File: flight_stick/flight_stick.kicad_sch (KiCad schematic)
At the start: 61 parts, among them J1 Load Cell 1, J10 USB_C_Receptacle_USB2.0, J11 Conn_01x05_Pin, J3 Load Cell 2, J5 Load Cell 3, J7 Conn_01x04_Male, J8 Conn_01x05_Pin, J9 Conn_ST_STDC14, Q4 2N7002, Q5 2N7002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

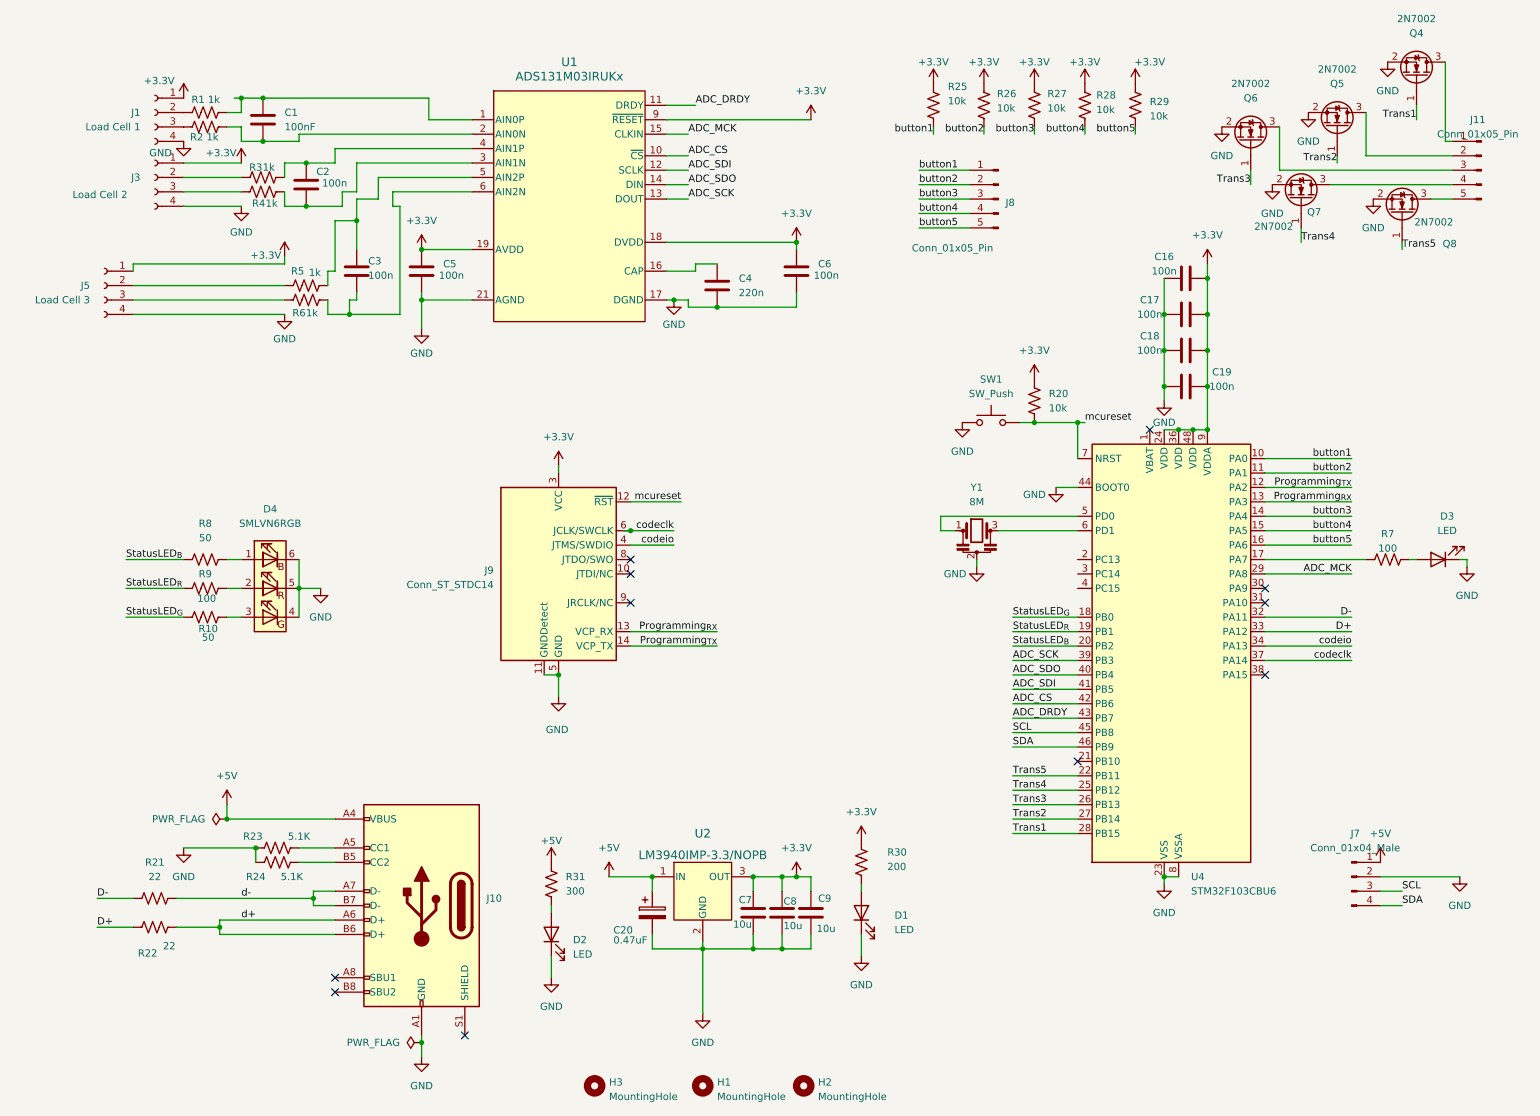
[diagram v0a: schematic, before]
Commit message: Updated Layout, Added Assembly part #s
Cleaned up layout for assembly minimum spacing

Added JLCPCB part #s for preorder and manufacturing
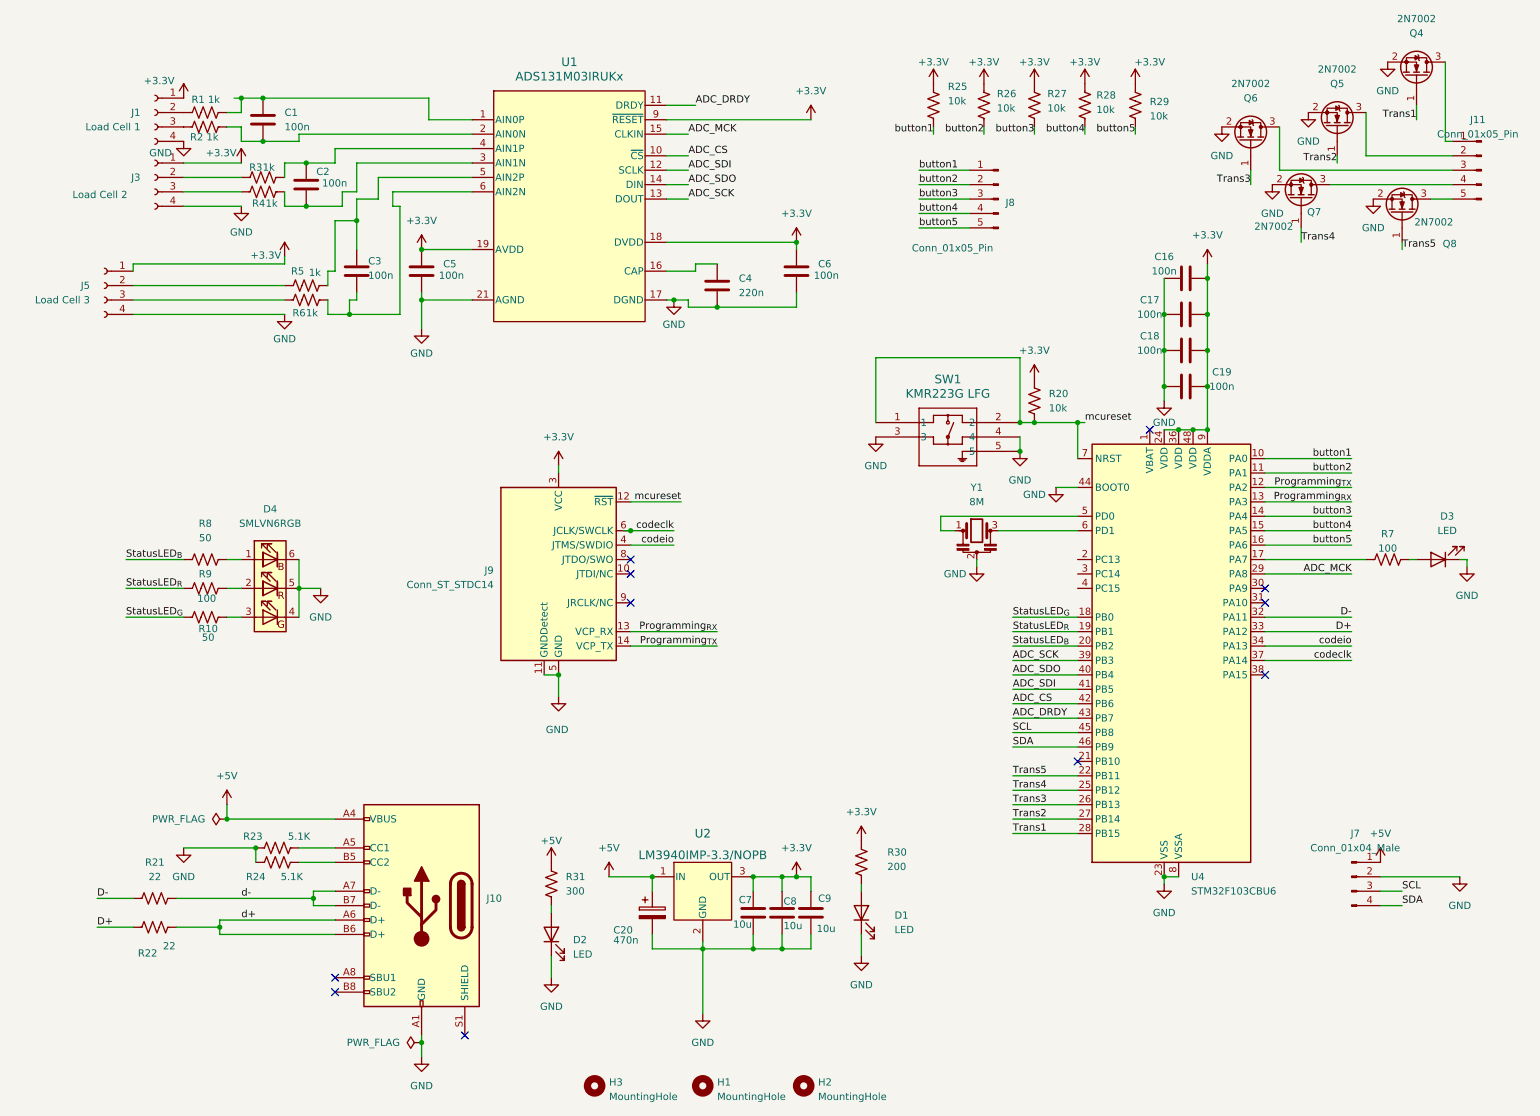
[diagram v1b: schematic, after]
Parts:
- removed SW1: SW_Push, Button_Switch_SMD:SW_Push_1P1T_NO_CK_KMR2, symbol Switch:SW_Push
- added SW1: KMR223G LFG, flight_stick_footprints:KMR2_G_CNK, symbol flight_stick:KMR223G_LFG
- C1: value 100nF -> 100n; LCSC (none) -> C116838
- C16, C17, C18, C19, C2, C3, C5, C6: LCSC (none) -> C116838
- C20: value 0.47uF -> 470n; LCSC (none) -> C106250
- C4: LCSC (none) -> C106857
- C7, C8, C9: LCSC (none) -> C90806
- D1: LCSC (none) -> C84256
- D2: LCSC (none) -> C965818
- D3: LCSC (none) -> C965815
- D4: LCSC (none) -> C2842809
- J1, J3, J5: LCSC (none) -> C5243684
- J10: LCSC (none) -> C165948
- J11, J8: LCSC (none) -> C124379
- J7: LCSC (none) -> C594232
- J9: LCSC (none) -> C2881912
- Q4, Q5, Q6, Q7, Q8: LCSC (none) -> C5224215
- R1, R2, R3, R4, R5, R6: LCSC (none) -> C73797
- R10, R8: LCSC (none) -> C849792
- R20, R25, R26, R27, R28, R29: LCSC (none) -> C25804
- R21, R22: LCSC (none) -> C23345
- R23, R24: LCSC (none) -> C23186
- R30: LCSC (none) -> C8218
- R31: LCSC (none) -> C23025
- R7, R9: LCSC (none) -> C105588
- U1: LCSC (none) -> C5116472
- U2: LCSC (none) -> C140319
- U4: LCSC (none) -> C55506
- Y1: LCSC (none) -> C341522
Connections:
- net AGND: now also SW1.3, SW1.4, SW1.5
- net mcureset: now also SW1.1, SW1.2

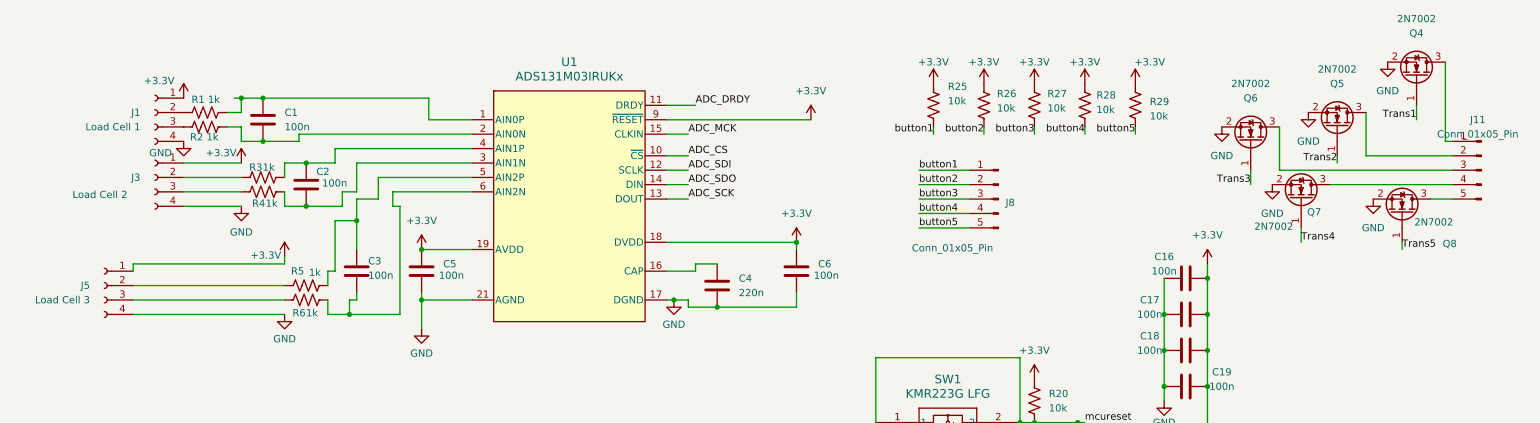
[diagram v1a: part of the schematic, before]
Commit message: Update production specifications of connectors and mounting holes
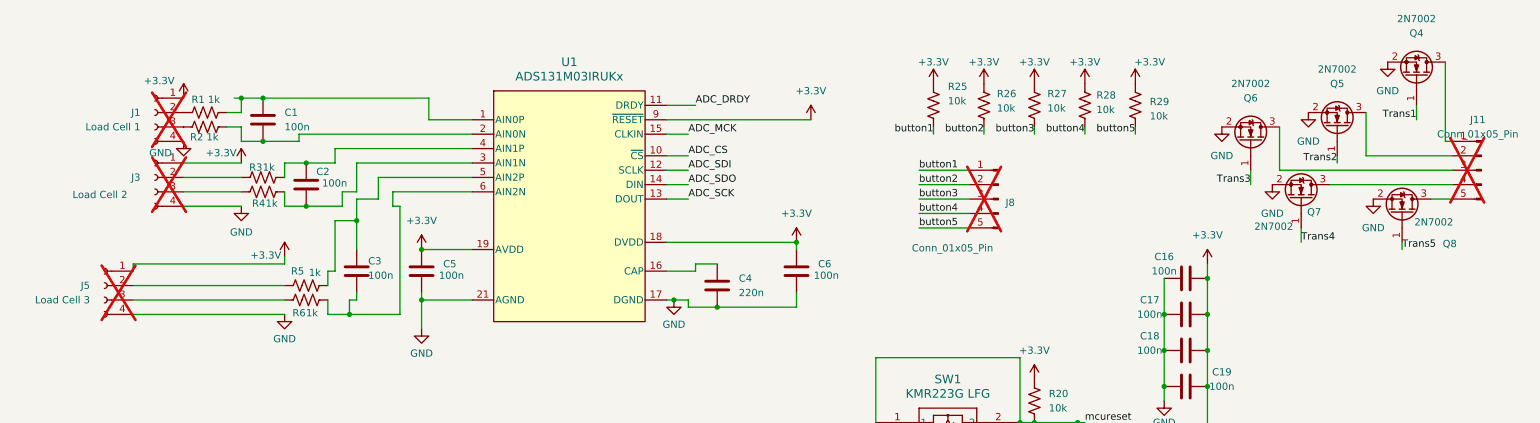
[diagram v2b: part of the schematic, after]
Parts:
- H1, H2, H3: now left out of the parts list
- J1, J11, J3, J5, J8: now not fitted
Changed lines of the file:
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@@
 		(in_bom yes)
 		(on_board yes)
-		(dnp no)
+		(dnp yes)
 		(property "Reference" "J5"
 			(at 16.51 59.69 0)
@@
 		(unit 1)
 		(exclude_from_sim no)
-		(in_bom yes)
+		(in_bom no)
 		(on_board yes)
 		(dnp no)
@@
 		(unit 1)
 		(exclude_from_sim no)
-		(in_bom yes)
+		(in_bom no)
 		(on_board yes)
 		(dnp no)
@@
 		(in_bom yes)
 		(on_board yes)
-		(dnp no)
+		(dnp yes)
 		(property "Reference" "J1"
 			(at 25.4 29.21 0)
@@
 		(in_bom yes)
 		(on_board yes)
-		(dnp no)
+		(dnp yes)
 		(property "Reference" "J3"
 			(at 25.4 40.64 0)
@@
 		(in_bom yes)
 		(on_board yes)
-		(dnp no)
+		(dnp yes)
 		(fields_autoplaced yes)
 		(property "Reference" "J11"
@@
 		(in_bom yes)
 		(on_board yes)
-		(dnp no)
+		(dnp yes)
 		(property "Reference" "J8"
 			(at 177.8 45.085 0)
@@
 		(unit 1)
 		(exclude_from_sim no)
-		(in_bom yes)
+		(in_bom no)
 		(on_board yes)
 		(dnp no)

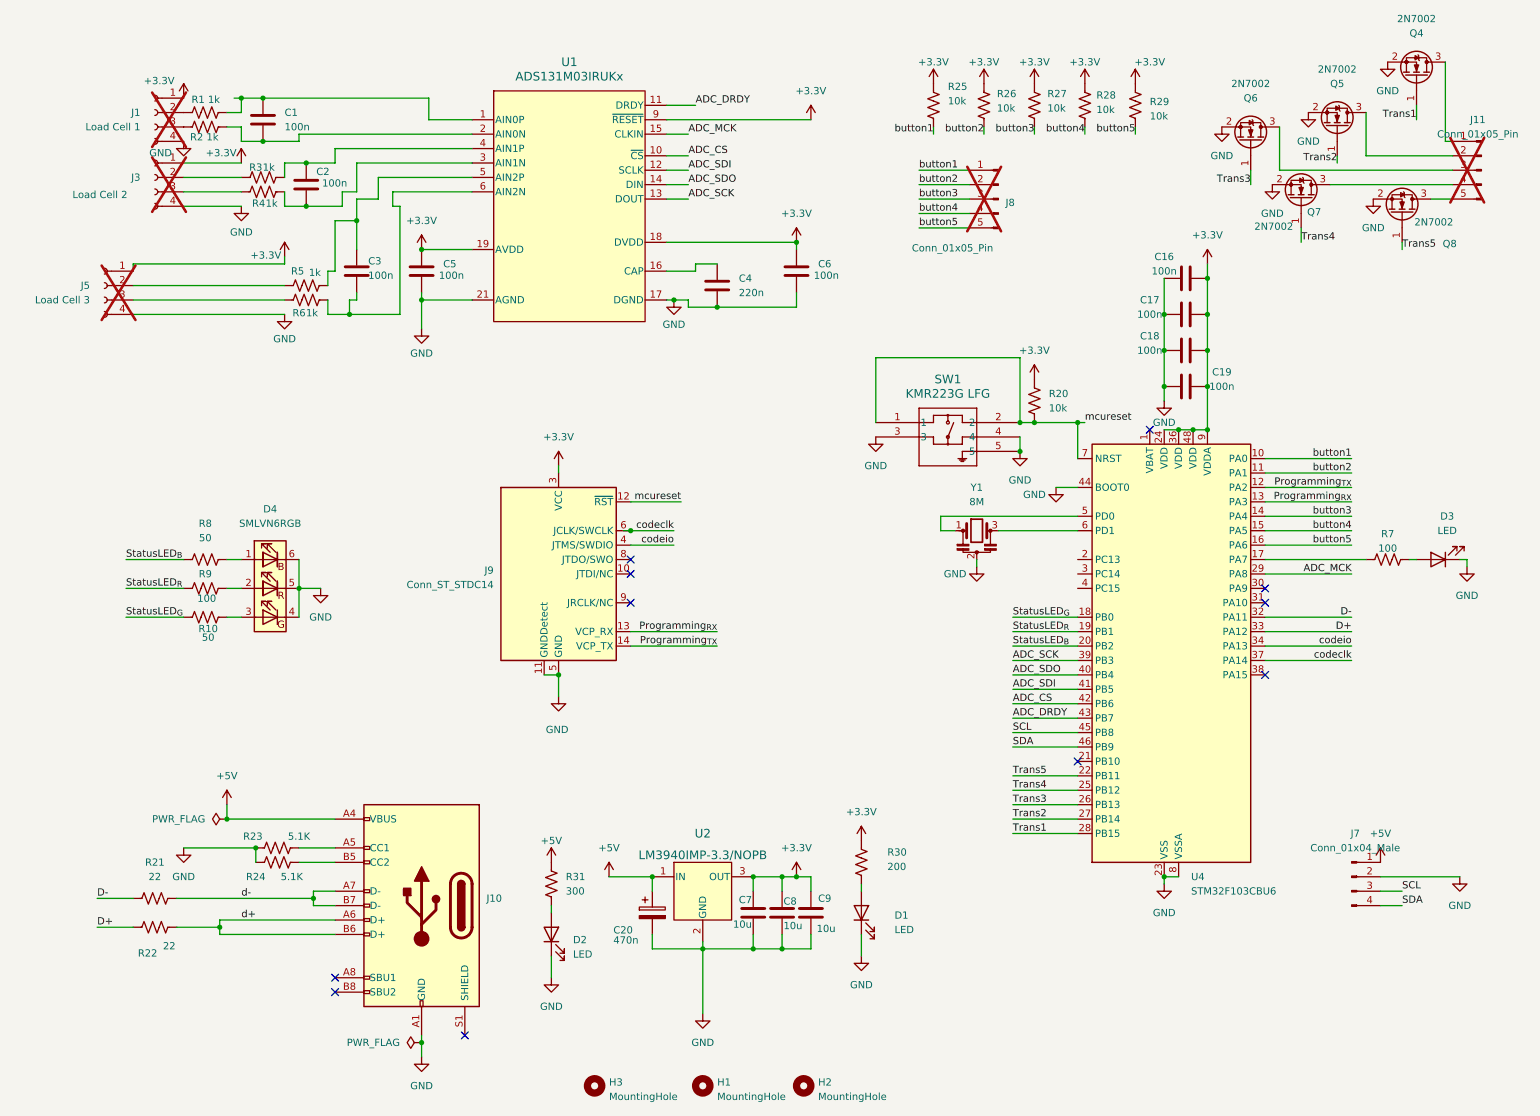
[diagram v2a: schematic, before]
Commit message: Created Draft of rev5 with CAN
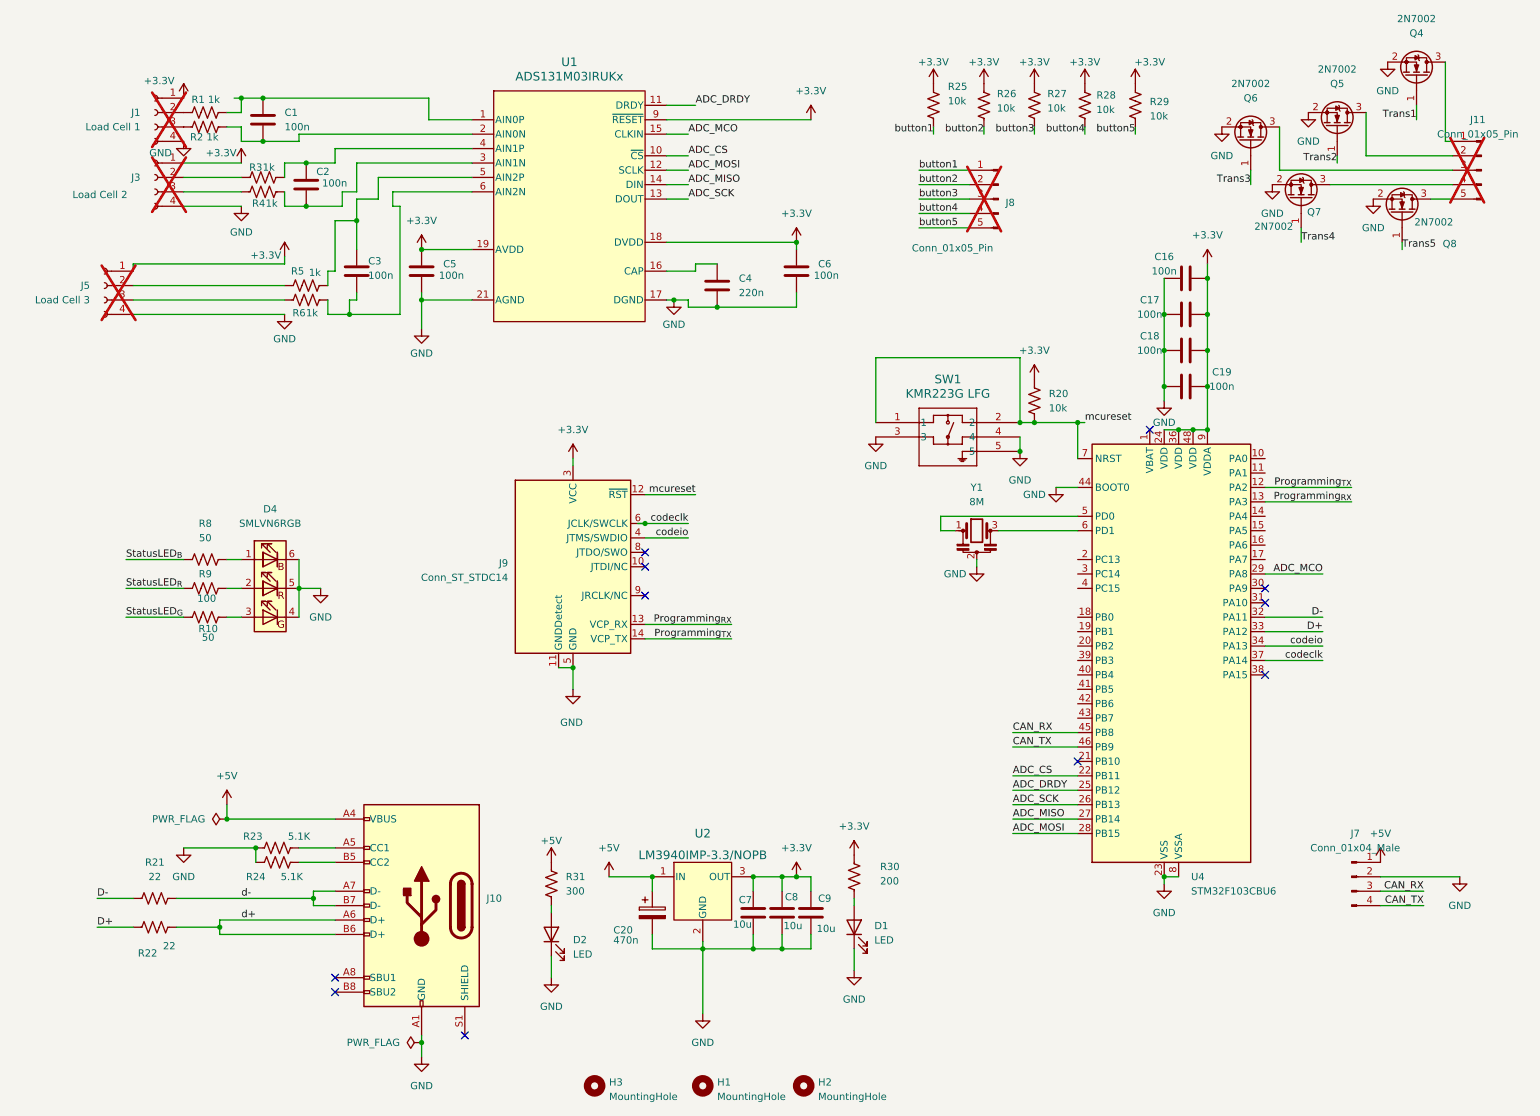
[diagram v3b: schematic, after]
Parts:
- removed D3: LED, LED_SMD:LED_0805_2012Metric, symbol Device:LED
- removed R7: 100, Resistor_SMD:R_0603_1608Metric, symbol Device:R_US
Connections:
- net ADC_CS: now also U4.22 (PB11); no longer U4.42 (PB6)
- net ADC_DRDY: now also U4.25 (PB12); no longer U4.43 (PB7)
- net ADC_SCK: now also U4.26 (PB13); no longer U4.39 (PB3)
- net StatusLED_{B}: no longer U4.20 (PB2)
- net StatusLED_{G}: no longer U4.18 (PB0)
- net StatusLED_{R}: no longer U4.19 (PB1)
- net Trans1: no longer U4.28 (PB15)
- net Trans2: no longer U4.27 (PB14)
- net Trans3: no longer U4.26 (PB13)
- net Trans4: no longer U4.25 (PB12)
- net Trans5: no longer U4.22 (PB11)
- net button1: no longer U4.10 (PA0)
- net button2: no longer U4.11 (PA1)
- net button3: no longer U4.14 (PA4)
- net button4: no longer U4.15 (PA5)
- net button5: no longer U4.16 (PA6)
- net ADC_MCK renamed ADC_MCO
- net ADC_SDI: no longer names the net of U4.41 (PB5)
- net ADC_SDI: no longer U1.12 (SCLK)
- net ADC_SDO: no longer names the net of U4.40 (PB4)
- net ADC_SDO: no longer U1.14 (DIN)
- net SCL renamed CAN_RX
- net SDA renamed CAN_TX
- new net ADC_MISO: U1.14 (DIN), U4.27 (PB14)
- new net ADC_MOSI: U1.12 (SCLK), U4.28 (PB15)
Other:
- moved on the sheet: D1, J9, R30
